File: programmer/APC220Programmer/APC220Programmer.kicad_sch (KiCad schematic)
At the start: 14 parts, among them Q1 2N7000, SW1 SW_SPST, SW2 Rotary_Encoder_Switch, U1 Adafruit BMP390 Module, U2 MPXH6115A6U/T1

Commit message: Minor improvements
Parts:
- BT1: footprint Connector_PinHeader_2.54mm:PinHeader_1x02_P2.54mm_Vertical -> Connector_Molex:Molex_KK-254_AE-6410-02A_1x02_P2.54mm_Vertical
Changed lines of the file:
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@@
 			)
 		)
-		(property "Footprint" "Connector_PinHeader_2.54mm:PinHeader_1x02_P2.54mm_Vertical"
+		(property "Footprint" "Connector_Molex:Molex_KK-254_AE-6410-02A_1x02_P2.54mm_Vertical"
 			(at 31.115 47.371 90)
 			(effects
@@
 			)
 		)
-		(property "Datasheet" "~"
+		(property "Datasheet" "https://www.molex.com/en-us/products/part-detail/22232021"
 			(at 31.115 47.371 90)
 			(effects

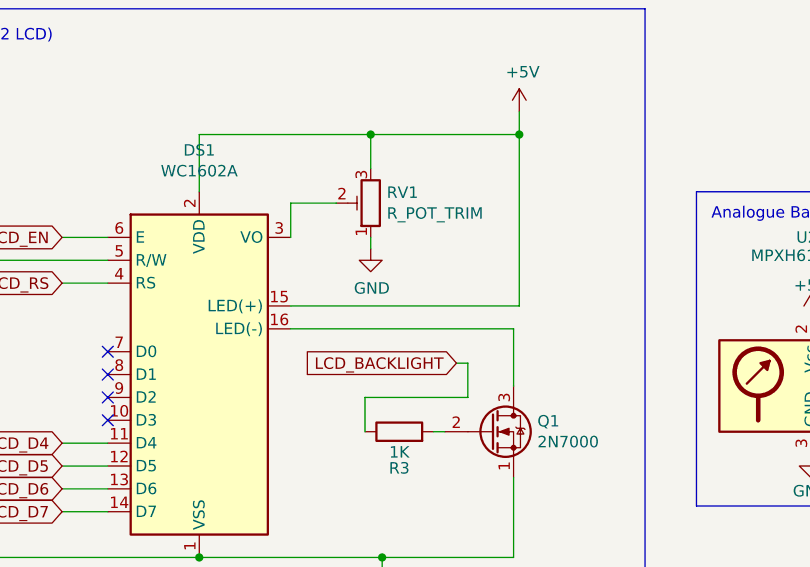
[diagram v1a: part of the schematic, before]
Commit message: Added current-limiting resistor for display backlight. Replaced rounded corners with square corners
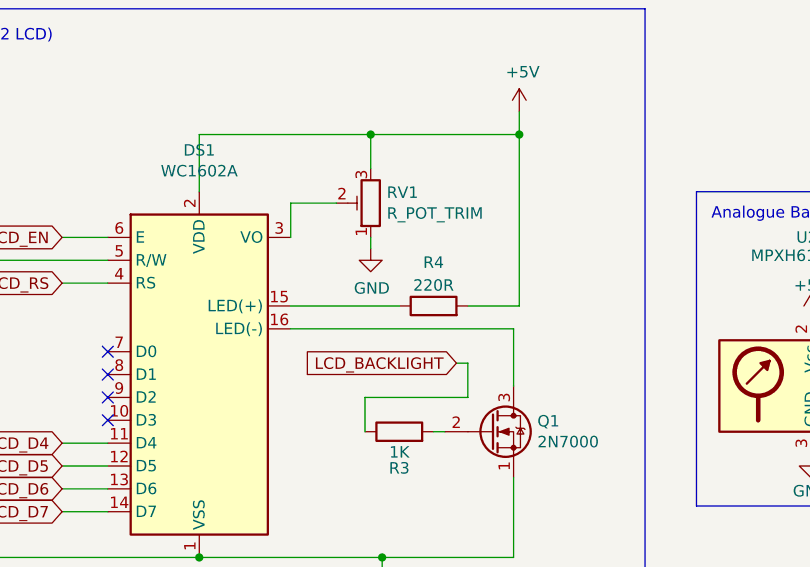
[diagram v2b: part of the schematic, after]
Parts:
- added R4: 220R, Resistor_THT:R_Axial_DIN0207_L6.3mm_D2.5mm_P10.16mm_Horizontal, symbol Device:R
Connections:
- net +5V: now also R4.2; no longer DS1.15 (LED(+))
- new net: DS1.15 (LED(+)), R4.1
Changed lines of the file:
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@@
 	(wire
 		(pts
-			(xy 69.215 142.24) (xy 94.615 142.24)
+			(xy 69.215 142.24) (xy 81.28 142.24)
 		)
 		(stroke
@@
 		(pts
 			(xy 157.48 152.4) (xy 157.48 162.56)
+		)
+		(stroke
+			(width 0)
+			(type default)
+		)
+	)
+	(wire
+		(pts
+			(xy 88.9 142.24) (xy 94.615 142.24)
 		)
 		(stroke
@@
 					(unit 1)
 				)
+			)
+		)
+	)
+	(symbol
+		(lib_id "Device:R")
+		(at 85.09 142.24 90)
+		(unit 1)
+		(exclude_from_sim no)
+		(in_bom yes)
+		(on_board yes)
+		(dnp no)
+		(property "Reference" "R4"
+			(at 85.09 137.414 90)
+			(effects
+				(font
+					(size 1.27 1.27)
+				)
+			)
+		)
+		(property "Value" "220R"
+			(at 85.09 139.954 90)
+			(effects
+				(font
+					(size 1.27 1.27)
+				)
+			)
+		)
+		(property "Footprint" "Resistor_THT:R_Axial_DIN0207_L6.3mm_D2.5mm_P10.16mm_Horizontal"
+			(at 85.09 144.018 90)
+			(effects
+				(font
+					(size 1.27 1.27)
+				)
+				(hide yes)
+			)
+		)
+		(property "Datasheet" "~"
+			(at 85.09 142.24 0)
+			(effects
+				(font
+					(size 1.27 1.27)
+				)
+				(hide yes)
+			)
+		)
+		(property "Description" "Resistor"
+			(at 85.09 142.24 0)
+			(effects
+				(font
+					(size 1.27 1.27)
+				)
+				(hide yes)
+			)
+		)
+		(pin "2"
+		)
+		(pin "1"
+		)
+		(instances
+			(project "APC220Programmer"
+				(path "/d0e4a882-7d08-4c2e-a090-dd49362d99ff"
+					(reference "R4")
+					(unit 1)
+				)
